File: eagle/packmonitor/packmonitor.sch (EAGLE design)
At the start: 33 parts, among them IC1 24C64, IC2 TCA4311A, IC3 AVRXDA32TQFP, IC4 ACS712

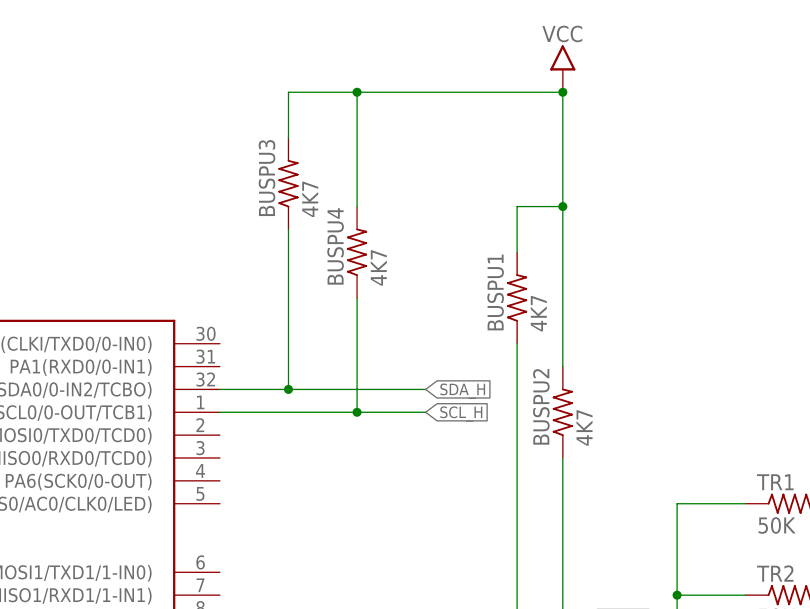
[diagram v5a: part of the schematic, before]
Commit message: Cleanup labels for new resistors
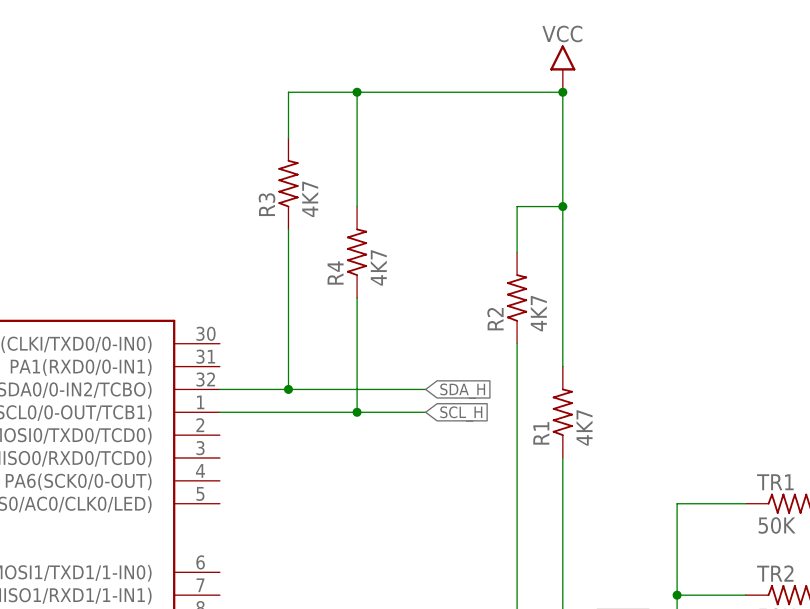
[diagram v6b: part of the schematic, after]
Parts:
- renumbered BUSPU1 to R2, BUSPU2 to R1, BUSPU3 to R3, BUSPU4 to R4
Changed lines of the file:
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@@
 <part name="RENA" library="rcl" deviceset="R-US_" device="R0603" value="10K"/>
 <part name="CACS1" library="rcl" deviceset="C-US" device="C0603" value="1n"/>
-<part name="BUSPU1" library="rcl" deviceset="R-US_" device="R0603" value="4K7"/>
-<part name="BUSPU2" library="rcl" deviceset="R-US_" device="R0603" value="4K7"/>
+<part name="R2" library="rcl" deviceset="R-US_" device="R0603" value="4K7"/>
+<part name="R1" library="rcl" deviceset="R-US_" device="R0603" value="4K7"/>
 <part name="U$4" library="bt" deviceset="VCC" device=""/>
-<part name="BUSPU3" library="rcl" deviceset="R-US_" device="R0603" value="4K7"/>
-<part name="BUSPU4" library="rcl" deviceset="R-US_" device="R0603" value="4K7"/>
+<part name="R3" library="rcl" deviceset="R-US_" device="R0603" value="4K7"/>
+<part name="R4" library="rcl" deviceset="R-US_" device="R0603" value="4K7"/>
 </parts>
 <sheets>
@@
 <instance part="RENA" gate="G$1" x="-33.02" y="55.88" rot="R90"/>
 <instance part="CACS1" gate="G$1" x="172.72" y="73.66"/>
-<instance part="BUSPU1" gate="G$1" x="124.46" y="190.5" rot="R90"/>
-<instance part="BUSPU2" gate="G$1" x="129.54" y="177.8" rot="R90"/>
+<instance part="R2" gate="G$1" x="124.46" y="190.5" rot="R90"/>
+<instance part="R1" gate="G$1" x="129.54" y="177.8" rot="R90"/>
 <instance part="U$4" gate="G$1" x="129.54" y="213.36"/>
-<instance part="BUSPU3" gate="G$1" x="99.06" y="203.2" rot="R90"/>
-<instance part="BUSPU4" gate="G$1" x="106.68" y="195.58" rot="R90"/>
+<instance part="R3" gate="G$1" x="99.06" y="203.2" rot="R90"/>
+<instance part="R4" gate="G$1" x="106.68" y="195.58" rot="R90"/>
 </instances>
 <busses>
@@
 </segment>
 <segment>
-<pinref part="BUSPU2" gate="G$1" pin="2"/>
+<pinref part="R1" gate="G$1" pin="2"/>
 <wire x1="129.54" y1="182.88" x2="129.54" y2="200.66" width="0.1524" layer="91"/>
-<pinref part="BUSPU1" gate="G$1" pin="2"/>
+<pinref part="R2" gate="G$1" pin="2"/>
 <wire x1="129.54" y1="200.66" x2="124.46" y2="200.66" width="0.1524" layer="91"/>
 <wire x1="124.46" y1="200.66" x2="124.46" y2="195.58" width="0.1524" layer="91"/>
@@
 <junction x="129.54" y="200.66"/>
 <pinref part="U$4" gate="G$1" pin="VCC"/>
-<pinref part="BUSPU3" gate="G$1" pin="2"/>
+<pinref part="R3" gate="G$1" pin="2"/>
 <wire x1="99.06" y1="208.28" x2="99.06" y2="213.36" width="0.1524" layer="91"/>
 <wire x1="99.06" y1="213.36" x2="106.68" y2="213.36" width="0.1524" layer="91"/>
 <junction x="129.54" y="213.36"/>
-<pinref part="BUSPU4" gate="G$1" pin="2"/>
+<pinref part="R4" gate="G$1" pin="2"/>
 <wire x1="106.68" y1="213.36" x2="129.54" y2="213.36" width="0.1524" layer="91"/>
 <wire x1="106.68" y1="200.66" x2="106.68" y2="213.36" width="0.1524" layer="91"/>
@@
 <label x="114.3" y="180.34" size="1.27" layer="95" xref="yes"/>
 <pinref part="IC3" gate="G$1" pin="PA2(SDA0/0-IN2/TCBO)"/>
-<pinref part="BUSPU3" gate="G$1" pin="1"/>
+<pinref part="R3" gate="G$1" pin="1"/>
 <wire x1="99.06" y1="180.34" x2="91.44" y2="180.34" width="0.1524" layer="91"/>
 <wire x1="99.06" y1="198.12" x2="99.06" y2="180.34" width="0.1524" layer="91"/>
@@
 <label x="114.3" y="177.8" size="1.27" layer="95" xref="yes"/>
 <pinref part="IC3" gate="G$1" pin="PA3(SCL0/0-OUT/TCB1)"/>
-<pinref part="BUSPU4" gate="G$1" pin="1"/>
+<pinref part="R4" gate="G$1" pin="1"/>
 <wire x1="106.68" y1="177.8" x2="91.44" y2="177.8" width="0.1524" layer="91"/>
 <wire x1="106.68" y1="190.5" x2="106.68" y2="177.8" width="0.1524" layer="91"/>
@@
 <wire x1="132.08" y1="154.94" x2="124.46" y2="154.94" width="0.1524" layer="91"/>
 <label x="132.08" y="154.94" size="1.27" layer="95" xref="yes"/>
-<pinref part="BUSPU1" gate="G$1" pin="1"/>
+<pinref part="R2" gate="G$1" pin="1"/>
 <wire x1="124.46" y1="154.94" x2="91.44" y2="154.94" width="0.1524" layer="91"/>
 <wire x1="124.46" y1="154.94" x2="124.46" y2="185.42" width="0.1524" layer="91"/>
@@
 <wire x1="132.08" y1="152.4" x2="129.54" y2="152.4" width="0.1524" layer="91"/>
 <label x="132.08" y="152.4" size="1.27" layer="95" xref="yes"/>
-<pinref part="BUSPU2" gate="G$1" pin="1"/>
+<pinref part="R1" gate="G$1" pin="1"/>
 <wire x1="129.54" y1="152.4" x2="91.44" y2="152.4" width="0.1524" layer="91"/>
 <wire x1="129.54" y1="152.4" x2="129.54" y2="172.72" width="0.1524" layer="91"/>

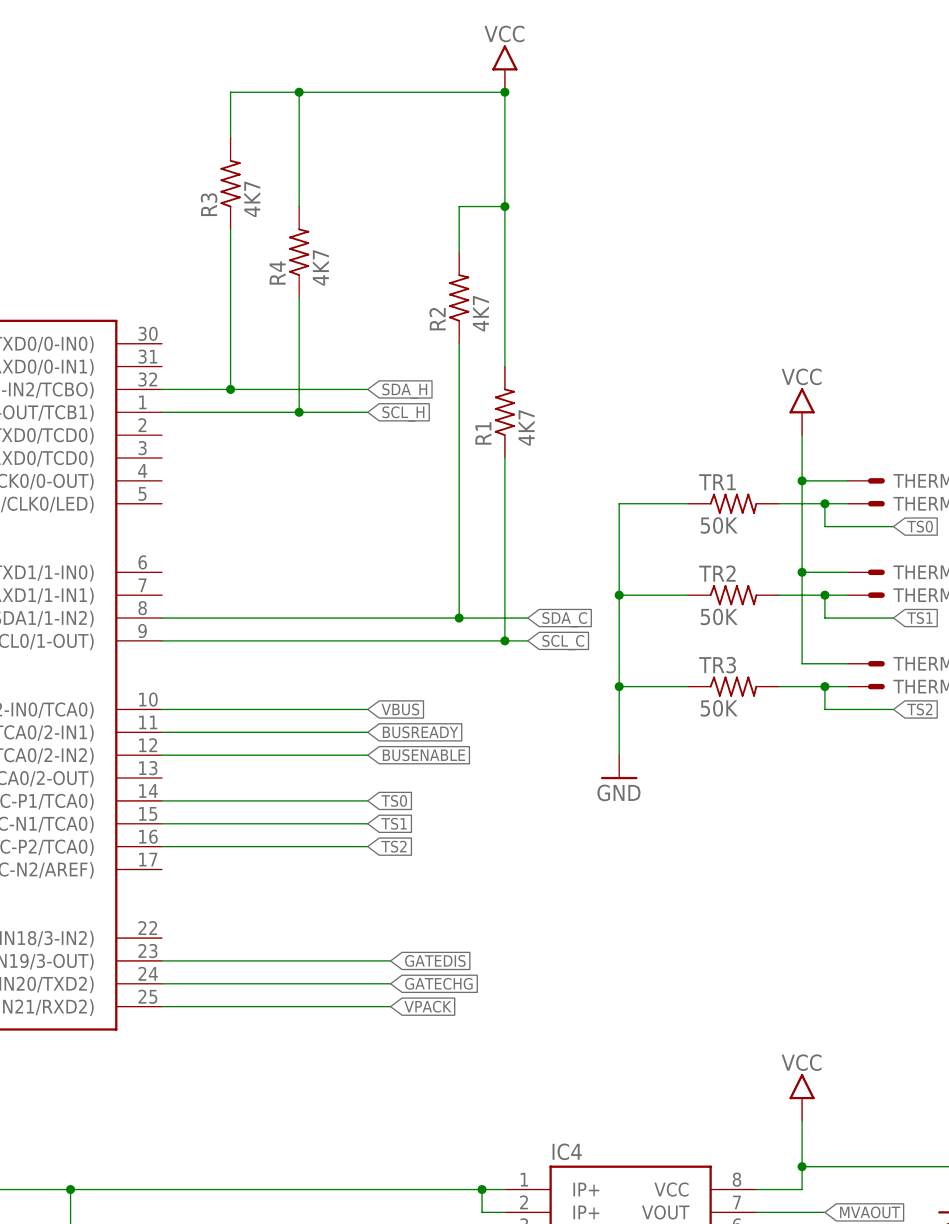
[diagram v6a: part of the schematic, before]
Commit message: Added prevision 2.5v reference, need to get the shoehorn.
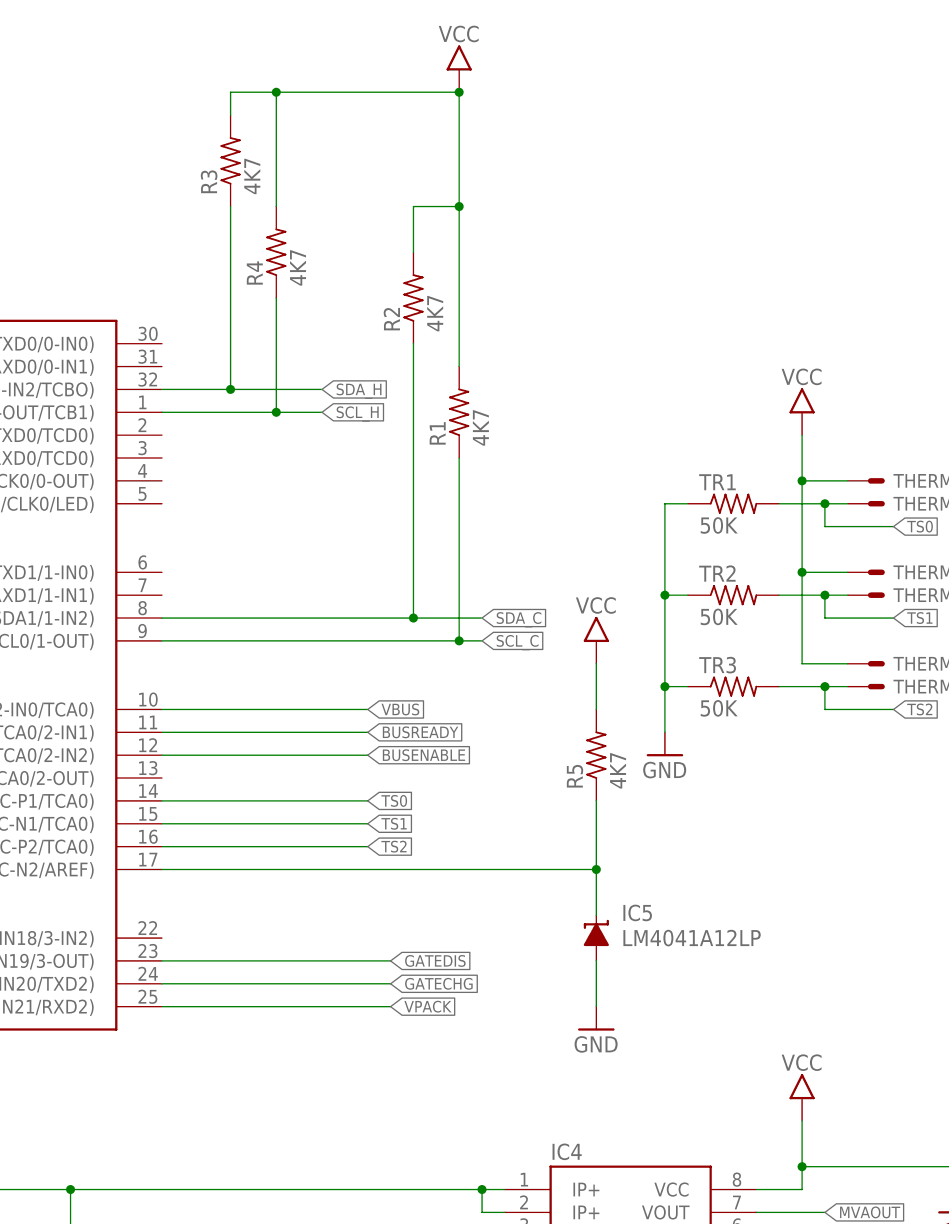
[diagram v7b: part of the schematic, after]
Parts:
- added IC5: LM4041A12LP, texas:LM4041A12LP
- added R5: 4K7, rcl:R-US_R0603
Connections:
- new net N$4: IC3.PD7(A7/AIN7/AC-N2/AREF), IC5.C, R5.1
- net GND: now also IC5.A
- net VCC: now also R5.2
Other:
- moved on the sheet: R1, R2, R3, R4
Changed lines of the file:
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@@
 <part name="R3" library="rcl" deviceset="R-US_" device="R0603" value="4K7"/>
 <part name="R4" library="rcl" deviceset="R-US_" device="R0603" value="4K7"/>
+<part name="IC5" library="texas" deviceset="LM4041" device="LP" technology="A12"/>
+<part name="R5" library="rcl" deviceset="R-US_" device="R0603" value="4K7"/>
+<part name="U$9" library="bt" deviceset="VCC" device=""/>
+<part name="GND7" library="bt" deviceset="GND" device=""/>
 </parts>
 <sheets>
@@
 <instance part="TR2" gate="G$1" x="154.94" y="157.48"/>
 <instance part="TR3" gate="G$1" x="154.94" y="147.32"/>
-<instance part="GND10" gate="1" x="142.24" y="137.16"/>
+<instance part="GND10" gate="1" x="147.32" y="139.7"/>
 <instance part="HOST_BUS" gate="-1" x="-71.12" y="86.36" rot="MR0"/>
 <instance part="HOST_BUS" gate="-2" x="-71.12" y="83.82" rot="MR0"/>
@@
 <instance part="RENA" gate="G$1" x="-33.02" y="55.88" rot="R90"/>
 <instance part="CACS1" gate="G$1" x="172.72" y="73.66"/>
-<instance part="R2" gate="G$1" x="124.46" y="190.5" rot="R90"/>
-<instance part="R1" gate="G$1" x="129.54" y="177.8" rot="R90"/>
-<instance part="U$4" gate="G$1" x="129.54" y="213.36"/>
-<instance part="R3" gate="G$1" x="99.06" y="203.2" rot="R90"/>
-<instance part="R4" gate="G$1" x="106.68" y="195.58" rot="R90"/>
+<instance part="R2" gate="G$1" x="119.38" y="190.5" rot="R90"/>
+<instance part="R1" gate="G$1" x="124.46" y="177.8" rot="R90"/>
+<instance part="U$4" gate="G$1" x="124.46" y="213.36"/>
+<instance part="R3" gate="G$1" x="99.06" y="205.74" rot="R90"/>
+<instance part="R4" gate="G$1" x="104.14" y="195.58" rot="R90"/>
+<instance part="IC5" gate="G$1" x="139.7" y="119.38"/>
+<instance part="R5" gate="G$1" x="139.7" y="139.7" rot="R90"/>
+<instance part="U$9" gate="G$1" x="139.7" y="149.86"/>
+<instance part="GND7" gate="1" x="139.7" y="109.22"/>
 </instances>
 <busses>
@@
 <segment>
 <pinref part="R1" gate="G$1" pin="2"/>
-<wire x1="129.54" y1="182.88" x2="129.54" y2="200.66" width="0.1524" layer="91"/>
+<wire x1="124.46" y1="182.88" x2="124.46" y2="200.66" width="0.1524" layer="91"/>
 <pinref part="R2" gate="G$1" pin="2"/>
-<wire x1="129.54" y1="200.66" x2="124.46" y2="200.66" width="0.1524" layer="91"/>
-<wire x1="124.46" y1="200.66" x2="124.46" y2="195.58" width="0.1524" layer="91"/>
-<wire x1="129.54" y1="200.66" x2="129.54" y2="213.36" width="0.1524" layer="91"/>
-<junction x="129.54" y="200.66"/>
+<wire x1="124.46" y1="200.66" x2="119.38" y2="200.66" width="0.1524" layer="91"/>
+<wire x1="119.38" y1="200.66" x2="119.38" y2="195.58" width="0.1524" layer="91"/>
+<wire x1="124.46" y1="200.66" x2="124.46" y2="213.36" width="0.1524" layer="91"/>
+<junction x="124.46" y="200.66"/>
 <pinref part="U$4" gate="G$1" pin="VCC"/>
 <pinref part="R3" gate="G$1" pin="2"/>
-<wire x1="99.06" y1="208.28" x2="99.06" y2="213.36" width="0.1524" layer="91"/>
-<wire x1="99.06" y1="213.36" x2="106.68" y2="213.36" width="0.1524" layer="91"/>
-<junction x="129.54" y="213.36"/>
+<wire x1="99.06" y1="210.82" x2="99.06" y2="213.36" width="0.1524" layer="91"/>
+<wire x1="99.06" y1="213.36" x2="104.14" y2="213.36" width="0.1524" layer="91"/>
+<junction x="124.46" y="213.36"/>
 <pinref part="R4" gate="G$1" pin="2"/>
-<wire x1="106.68" y1="213.36" x2="129.54" y2="213.36" width="0.1524" layer="91"/>
-<wire x1="106.68" y1="200.66" x2="106.68" y2="213.36" width="0.1524" layer="91"/>
-<junction x="106.68" y="213.36"/>
+<wire x1="104.14" y1="213.36" x2="124.46" y2="213.36" width="0.1524" layer="91"/>
+<wire x1="104.14" y1="200.66" x2="104.14" y2="213.36" width="0.1524" layer="91"/>
+<junction x="104.14" y="213.36"/>
+</segment>
+<segment>
+<pinref part="R5" gate="G$1" pin="2"/>
+<pinref part="U$9" gate="G$1" pin="VCC"/>
+<wire x1="139.7" y1="144.78" x2="139.7" y2="149.86" width="0.1524" layer="91"/>
 </segment>
 </net>
@@
 <pinref part="TR3" gate="G$1" pin="1"/>
 <pinref part="GND10" gate="1" pin="GND"/>
-<wire x1="149.86" y1="147.32" x2="142.24" y2="147.32" width="0.1524" layer="91"/>
-<wire x1="142.24" y1="147.32" x2="142.24" y2="139.7" width="0.1524" layer="91"/>
+<wire x1="149.86" y1="147.32" x2="147.32" y2="147.32" width="0.1524" layer="91"/>
+<wire x1="147.32" y1="147.32" x2="147.32" y2="142.24" width="0.1524" layer="91"/>
 <pinref part="TR2" gate="G$1" pin="1"/>
-<wire x1="149.86" y1="157.48" x2="142.24" y2="157.48" width="0.1524" layer="91"/>
-<wire x1="142.24" y1="157.48" x2="142.24" y2="147.32" width="0.1524" layer="91"/>
-<junction x="142.24" y="147.32"/>
+<wire x1="149.86" y1="157.48" x2="147.32" y2="157.48" width="0.1524" layer="91"/>
+<wire x1="147.32" y1="157.48" x2="147.32" y2="147.32" width="0.1524" layer="91"/>
+<junction x="147.32" y="147.32"/>
 <pinref part="TR1" gate="G$1" pin="1"/>
-<wire x1="149.86" y1="167.64" x2="142.24" y2="167.64" width="0.1524" layer="91"/>
-<wire x1="142.24" y1="167.64" x2="142.24" y2="157.48" width="0.1524" layer="91"/>
-<junction x="142.24" y="157.48"/>
+<wire x1="149.86" y1="167.64" x2="147.32" y2="167.64" width="0.1524" layer="91"/>
+<wire x1="147.32" y1="167.64" x2="147.32" y2="157.48" width="0.1524" layer="91"/>
+<junction x="147.32" y="157.48"/>
 </segment>
 <segment>
@@
 <wire x1="83.82" y1="68.58" x2="81.28" y2="68.58" width="0.1524" layer="91"/>
 <junction x="81.28" y="68.58"/>
+</segment>
+<segment>
+<pinref part="IC5" gate="G$1" pin="A"/>
+<pinref part="GND7" gate="1" pin="GND"/>
+<wire x1="139.7" y1="116.84" x2="139.7" y2="111.76" width="0.1524" layer="91"/>
 </segment>
 </net>
@@
 <net name="SDA_H" class="0">
 <segment>
-<wire x1="114.3" y1="180.34" x2="99.06" y2="180.34" width="0.1524" layer="91"/>
-<label x="114.3" y="180.34" size="1.27" layer="95" xref="yes"/>
+<wire x1="109.22" y1="180.34" x2="99.06" y2="180.34" width="0.1524" layer="91"/>
+<label x="109.22" y="180.34" size="1.27" layer="95" xref="yes"/>
 <pinref part="IC3" gate="G$1" pin="PA2(SDA0/0-IN2/TCBO)"/>
 <pinref part="R3" gate="G$1" pin="1"/>
 <wire x1="99.06" y1="180.34" x2="91.44" y2="180.34" width="0.1524" layer="91"/>
-<wire x1="99.06" y1="198.12" x2="99.06" y2="180.34" width="0.1524" layer="91"/>
+<wire x1="99.06" y1="200.66" x2="99.06" y2="180.34" width="0.1524" layer="91"/>
 <junction x="99.06" y="180.34"/>
 </segment>
@@
 <net name="SCL_H" class="0">
 <segment>
-<wire x1="114.3" y1="177.8" x2="106.68" y2="177.8" width="0.1524" layer="91"/>
-<label x="114.3" y="177.8" size="1.27" layer="95" xref="yes"/>
+<wire x1="109.22" y1="177.8" x2="104.14" y2="177.8" width="0.1524" layer="91"/>
+<label x="109.22" y="177.8" size="1.27" layer="95" xref="yes"/>
 <pinref part="IC3" gate="G$1" pin="PA3(SCL0/0-OUT/TCB1)"/>
 <pinref part="R4" gate="G$1" pin="1"/>
-<wire x1="106.68" y1="177.8" x2="91.44" y2="177.8" width="0.1524" layer="91"/>
-<wire x1="106.68" y1="190.5" x2="106.68" y2="177.8" width="0.1524" layer="91"/>
-<junction x="106.68" y="177.8"/>
+<wire x1="104.14" y1="177.8" x2="91.44" y2="177.8" width="0.1524" layer="91"/>
+<wire x1="104.14" y1="190.5" x2="104.14" y2="177.8" width="0.1524" layer="91"/>
+<junction x="104.14" y="177.8"/>
 </segment>
 <segment>
@@
 <segment>
 <pinref part="IC3" gate="G$1" pin="PC2(SCK1/SDA1/1-IN2)"/>
-<wire x1="132.08" y1="154.94" x2="124.46" y2="154.94" width="0.1524" layer="91"/>
-<label x="132.08" y="154.94" size="1.27" layer="95" xref="yes"/>
+<wire x1="127" y1="154.94" x2="119.38" y2="154.94" width="0.1524" layer="91"/>
+<label x="127" y="154.94" size="1.27" layer="95" xref="yes"/>
 <pinref part="R2" gate="G$1" pin="1"/>
-<wire x1="124.46" y1="154.94" x2="91.44" y2="154.94" width="0.1524" layer="91"/>
-<wire x1="124.46" y1="154.94" x2="124.46" y2="185.42" width="0.1524" layer="91"/>
-<junction x="124.46" y="154.94"/>
+<wire x1="119.38" y1="154.94" x2="91.44" y2="154.94" width="0.1524" layer="91"/>
+<wire x1="119.38" y1="154.94" x2="119.38" y2="185.42" width="0.1524" layer="91"/>
+<junction x="119.38" y="154.94"/>
 </segment>
 <segment>
@@
 <segment>
 <pinref part="IC3" gate="G$1" pin="PC3(SS1/SCL0/1-OUT)"/>
-<wire x1="132.08" y1="152.4" x2="129.54" y2="152.4" width="0.1524" layer="91"/>
-<label x="132.08" y="152.4" size="1.27" layer="95" xref="yes"/>
+<wire x1="127" y1="152.4" x2="124.46" y2="152.4" width="0.1524" layer="91"/>
+<label x="127" y="152.4" size="1.27" layer="95" xref="yes"/>
 <pinref part="R1" gate="G$1" pin="1"/>
-<wire x1="129.54" y1="152.4" x2="91.44" y2="152.4" width="0.1524" layer="91"/>
-<wire x1="129.54" y1="152.4" x2="129.54" y2="172.72" width="0.1524" layer="91"/>
-<junction x="129.54" y="152.4"/>
+<wire x1="124.46" y1="152.4" x2="91.44" y2="152.4" width="0.1524" layer="91"/>
+<wire x1="124.46" y1="152.4" x2="124.46" y2="172.72" width="0.1524" layer="91"/>
+<junction x="124.46" y="152.4"/>
 </segment>
 <segment>
@@
 </segment>
 </net>
+<net name="N$4" class="0">
+<segment>
+<pinref part="IC3" gate="G$1" pin="PD7(A7/AIN7/AC-N2/AREF)"/>
+<pinref part="IC5" gate="G$1" pin="C"/>
+<wire x1="91.44" y1="127" x2="139.7" y2="127" width="0.1524" layer="91"/>
+<wire x1="139.7" y1="127" x2="139.7" y2="121.92" width="0.1524" layer="91"/>
+<pinref part="R5" gate="G$1" pin="1"/>
+<wire x1="139.7" y1="127" x2="139.7" y2="134.62" width="0.1524" layer="91"/>
+<junction x="139.7" y="127"/>
+</segment>
+</net>
